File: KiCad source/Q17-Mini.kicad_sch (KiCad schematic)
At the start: 80 parts, among them J1 Input, J2-1 SPK+, J2-2 SPK-, J3-1 V+, J3-2 GND, J3-3 V-, Q1 IRF610, Q10 KSA992, Q11 BS250P, Q12 BD139, Q13 IRF610, Q14 IRF9610, Q15 FQA46N15, Q16 FQA36P15, Q2 KSA992, Q3 KSC1845, Q4 IRF9610, Q5 FQP3P20, Q6 FQP3N30, Q7 KSC1845, Q8 ZVN4206AV, Q9 BS250P, U1 OPA1641

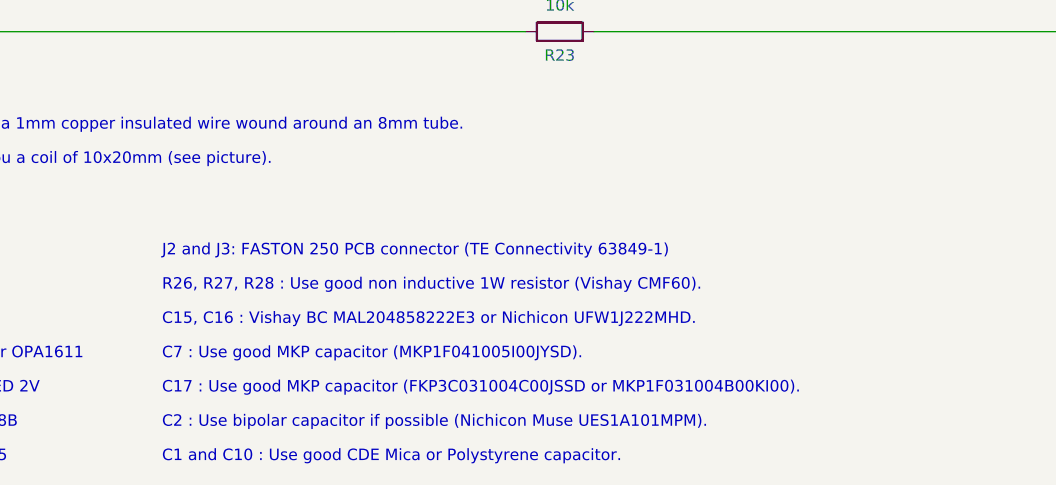
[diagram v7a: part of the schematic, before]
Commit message: PCB v1.0.9
Moved Q15 and Q16 inward a bit to change the border track to 3mm.
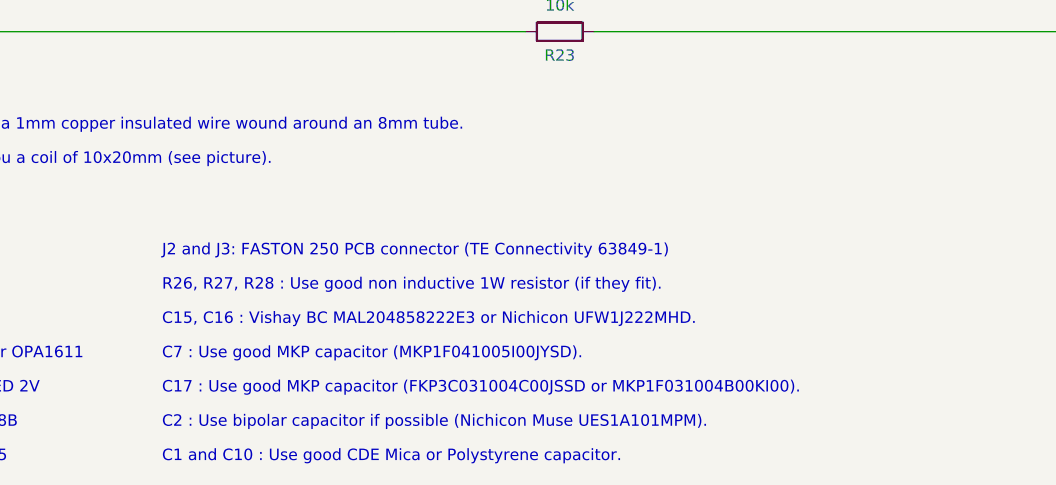
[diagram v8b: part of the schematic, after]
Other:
- note added: "R26, R27, R28 : Use good non inductive 1W resistor (if they fit)."
- note removed: "R26, R27, R28 : Use good non inductive 1W resistor (Vishay CMF60)."
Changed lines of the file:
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@@
     (effects (font (size 1.27 1.27)) (justify left bottom))
   )
-  (text "R26, R27, R28 : Use good non inductive 1W resistor (Vishay CMF60)."
+  (text "R26, R27, R28 : Use good non inductive 1W resistor (if they fit)."
     (at 93.98 177.8 0)
     (effects (font (size 1.27 1.27)) (justify left bottom))
